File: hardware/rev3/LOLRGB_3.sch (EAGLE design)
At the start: 77 parts, among them Q1 BSS138

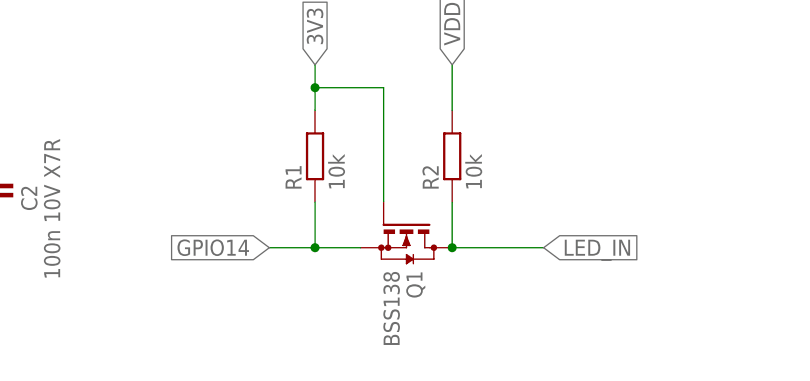
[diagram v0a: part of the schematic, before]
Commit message: SOT23-Footprint changed
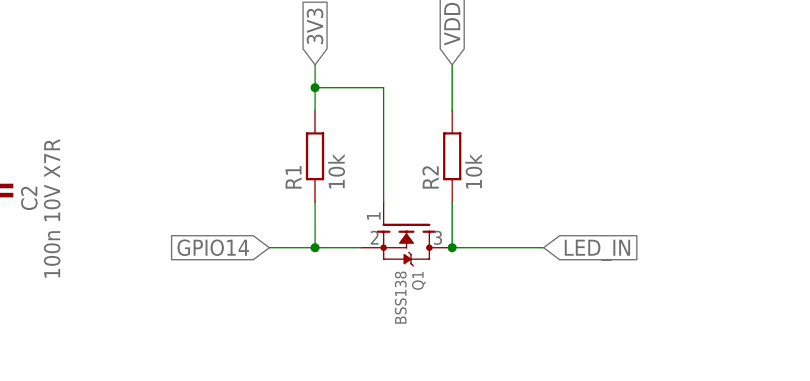
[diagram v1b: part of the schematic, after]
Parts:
- Q1: device transistor-small-signal:BSS123 -> adafruit:MOSFET-NSOT23R
